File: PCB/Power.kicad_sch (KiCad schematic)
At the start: 9 parts, among them U3 XL1509-3.3

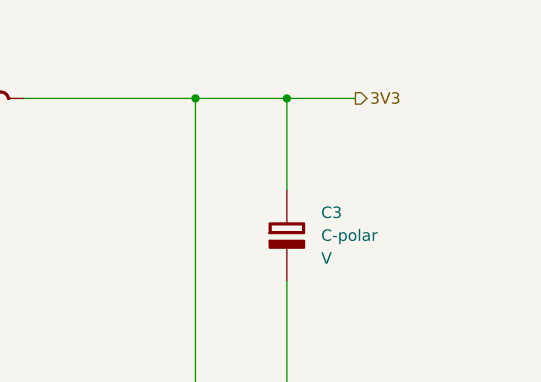
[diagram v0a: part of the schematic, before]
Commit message: Updated PCB. Added Debug section and rectifed RS485
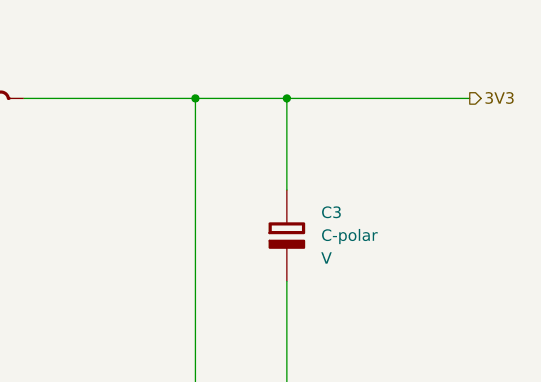
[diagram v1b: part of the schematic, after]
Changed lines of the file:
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@@
 	(wire
 		(pts
-			(xy 223.52 71.12) (xy 231.14 71.12)
+			(xy 223.52 71.12) (xy 243.84 71.12)
 		)
 		(stroke
@@
 	(hierarchical_label "3V3"
 		(shape output)
-		(at 231.14 71.12 0)
+		(at 243.84 71.12 0)
 		(fields_autoplaced yes)
 		(effects

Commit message: Updated PCB.
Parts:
- renumbered C1 to C14, C2 to C15, C4 to C16, C3 to C17, L1 to L2, R2 to R12, R1 to R13, U3 to U4
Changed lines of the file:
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@@
 		(dnp no)
 		(fields_autoplaced yes)
-		(property "Reference" "#PWR05"
+		(property "Reference" "#PWR022"
 			(at 110.49 127 0)
 			(effects
@@
 		(instances
 			(project "IMU_V100"
-				(path "/b6a8d14b-6e32-4628-bf0c-2046877d1cfa/af1be3cc-4748-49ee-b74b-ab259917e083"
-					(reference "#PWR05")
+				(path "/b6a8d14b-6e32-4628-bf0c-2046877d1cfa/205555cc-3b86-4915-975e-3a7e3eed6661/f9424131-b250-4638-a784-b5462b05c1af"
+					(reference "#PWR022")
 					(unit 1)
 				)
@@
 		(dnp no)
 		(fields_autoplaced yes)
-		(property "Reference" "C4"
+		(property "Reference" "C16"
 			(at 196.85 132.08 90)
 			(effects
@@
 		(instances
 			(project "IMU_V100"
-				(path "/b6a8d14b-6e32-4628-bf0c-2046877d1cfa/af1be3cc-4748-49ee-b74b-ab259917e083"
-					(reference "C4")
+				(path "/b6a8d14b-6e32-4628-bf0c-2046877d1cfa/205555cc-3b86-4915-975e-3a7e3eed6661/f9424131-b250-4638-a784-b5462b05c1af"
+					(reference "C16")
 					(unit 1)
 				)
@@
 		(dnp no)
 		(fields_autoplaced yes)
-		(property "Reference" "L1"
+		(property "Reference" "L2"
 			(at 189.23 64.77 90)
 			(effects
@@
 		)
 		(instances
-			(project ""
-				(path "/b6a8d14b-6e32-4628-bf0c-2046877d1cfa/af1be3cc-4748-49ee-b74b-ab259917e083"
-					(reference "L1")
+			(project "IMU_V100"
+				(path "/b6a8d14b-6e32-4628-bf0c-2046877d1cfa/205555cc-3b86-4915-975e-3a7e3eed6661/f9424131-b250-4638-a784-b5462b05c1af"
+					(reference "L2")
 					(unit 1)
 				)
@@
 		(dnp no)
 		(fields_autoplaced yes)
-		(property "Reference" "#PWR03"
+		(property "Reference" "#PWR024"
 			(at 170.18 111.76 0)
 			(effects
@@
 		(instances
 			(project "IMU_V100"
-				(path "/b6a8d14b-6e32-4628-bf0c-2046877d1cfa/af1be3cc-4748-49ee-b74b-ab259917e083"
-					(reference "#PWR03")
+				(path "/b6a8d14b-6e32-4628-bf0c-2046877d1cfa/205555cc-3b86-4915-975e-3a7e3eed6661/f9424131-b250-4638-a784-b5462b05c1af"
+					(reference "#PWR024")
 					(unit 1)
 				)
@@
 		(dnp no)
 		(fields_autoplaced yes)
-		(property "Reference" "C3"
+		(property "Reference" "C17"
 			(at 227.33 83.8199 0)
 			(effects
@@
 		(instances
 			(project "IMU_V100"
-				(path "/b6a8d14b-6e32-4628-bf0c-2046877d1cfa/af1be3cc-4748-49ee-b74b-ab259917e083"
-					(reference "C3")
+				(path "/b6a8d14b-6e32-4628-bf0c-2046877d1cfa/205555cc-3b86-4915-975e-3a7e3eed6661/f9424131-b250-4638-a784-b5462b05c1af"
+					(reference "C17")
 					(unit 1)
 				)
@@
 		(dnp no)
 		(fields_autoplaced yes)
-		(property "Reference" "U3"
+		(property "Reference" "U4"
 			(at 128.27 63.5 0)
 			(effects
@@
 		)
 		(instances
-			(project ""
-				(path "/b6a8d14b-6e32-4628-bf0c-2046877d1cfa/af1be3cc-4748-49ee-b74b-ab259917e083"
-					(reference "U3")
+			(project "IMU_V100"
+				(path "/b6a8d14b-6e32-4628-bf0c-2046877d1cfa/205555cc-3b86-4915-975e-3a7e3eed6661/f9424131-b250-4638-a784-b5462b05c1af"
+					(reference "U4")
 					(unit 1)
 				)
@@
 		(dnp no)
 		(fields_autoplaced yes)
-		(property "Reference" "R2"
+		(property "Reference" "R12"
 			(at 137.16 123.19 90)
 			(effects
@@
 		(instances
 			(project "IMU_V100"
-				(path "/b6a8d14b-6e32-4628-bf0c-2046877d1cfa/af1be3cc-4748-49ee-b74b-ab259917e083"
-					(reference "R2")
+				(path "/b6a8d14b-6e32-4628-bf0c-2046877d1cfa/205555cc-3b86-4915-975e-3a7e3eed6661/f9424131-b250-4638-a784-b5462b05c1af"
+					(reference "R12")
 					(unit 1)
 				)
@@
 		(dnp no)
 		(fields_autoplaced yes)
-		(property "Reference" "#PWR01"
+		(property "Reference" "#PWR023"
 			(at 128.27 93.98 0)
 			(effects
@@
 		)
 		(instances
-			(project ""
-				(path "/b6a8d14b-6e32-4628-bf0c-2046877d1cfa/af1be3cc-4748-49ee-b74b-ab259917e083"
-					(reference "#PWR01")
+			(project "IMU_V100"
+				(path "/b6a8d14b-6e32-4628-bf0c-2046877d1cfa/205555cc-3b86-4915-975e-3a7e3eed6661/f9424131-b250-4638-a784-b5462b05c1af"
+					(reference "#PWR023")
 					(unit 1)
 				)
@@
 		(dnp no)
 		(fields_autoplaced yes)
-		(property "Reference" "R1"
+		(property "Reference" "R13"
 			(at 196.85 123.19 90)
 			(effects
@@
 		)
 		(instances
-			(project ""
-				(path "/b6a8d14b-6e32-4628-bf0c-2046877d1cfa/af1be3cc-4748-49ee-b74b-ab259917e083"
-					(reference "R1")
+			(project "IMU_V100"
+				(path "/b6a8d14b-6e32-4628-bf0c-2046877d1cfa/205555cc-3b86-4915-975e-3a7e3eed6661/f9424131-b250-4638-a784-b5462b05c1af"
+					(reference "R13")
 					(unit 1)
 				)
@@
 		)
 		(instances
-			(project ""
-				(path "/b6a8d14b-6e32-4628-bf0c-2046877d1cfa/af1be3cc-4748-49ee-b74b-ab259917e083"
+			(project "IMU_V100"
+				(path "/b6a8d14b-6e32-4628-bf0c-2046877d1cfa/205555cc-3b86-4915-975e-3a7e3eed6661/f9424131-b250-4638-a784-b5462b05c1af"
 					(reference "DZ1")
 					(unit 1)
@@
 		(dnp no)
 		(fields_autoplaced yes)
-		(property "Reference" "C2"
+		(property "Reference" "C15"
 			(at 102.87 85.0899 0)
 			(effects
@@
 		)
 		(instances
-			(project ""
-				(path "/b6a8d14b-6e32-4628-bf0c-2046877d1cfa/af1be3cc-4748-49ee-b74b-ab259917e083"
-					(reference "C2")
+			(project "IMU_V100"
+				(path "/b6a8d14b-6e32-4628-bf0c-2046877d1cfa/205555cc-3b86-4915-975e-3a7e3eed6661/f9424131-b250-4638-a784-b5462b05c1af"
+					(reference "C15")
 					(unit 1)
 				)
@@
 		(dnp no)
 		(fields_autoplaced yes)
-		(property "Reference" "C1"
+		(property "Reference" "C14"
 			(at 85.09 83.8199 0)
 			(effects
@@
 		)
 		(instances
-			(project ""
-				(path "/b6a8d14b-6e32-4628-bf0c-2046877d1cfa/af1be3cc-4748-49ee-b74b-ab259917e083"
-					(reference "C1")
+			(project "IMU_V100"
+				(path "/b6a8d14b-6e32-4628-bf0c-2046877d1cfa/205555cc-3b86-4915-975e-3a7e3eed6661/f9424131-b250-4638-a784-b5462b05c1af"
+					(reference "C14")
 					(unit 1)
 				)
@@
 		(dnp no)
 		(fields_autoplaced yes)
-		(property "Reference" "#PWR04"
+		(property "Reference" "#PWR025"
 			(at 223.52 111.76 0)
 			(effects
@@
 		(instances
 			(project "IMU_V100"
-				(path "/b6a8d14b-6e32-4628-bf0c-2046877d1cfa/af1be3cc-4748-49ee-b74b-ab259917e083"
-					(reference "#PWR04")
+				(path "/b6a8d14b-6e32-4628-bf0c-2046877d1cfa/205555cc-3b86-4915-975e-3a7e3eed6661/f9424131-b250-4638-a784-b5462b05c1af"
+					(reference "#PWR025")
 					(unit 1)
 				)
@@
 		(dnp no)
 		(fields_autoplaced yes)
-		(property "Reference" "#PWR02"
+		(property "Reference" "#PWR021"
 			(at 90.17 115.57 0)
 			(effects
@@
 		(instances
 			(project "IMU_V100"
-				(path "/b6a8d14b-6e32-4628-bf0c-2046877d1cfa/af1be3cc-4748-49ee-b74b-ab259917e083"
-					(reference "#PWR02")
-					(unit 1)
-				)
+				(path "/b6a8d14b-6e32-4628-bf0c-2046877d1cfa/205555cc-3b86-4915-975e-3a7e3eed6661/f9424131-b250-4638-a784-b5462b05c1af"
+					(reference "#PWR021")
+					(unit 1)
+				)
